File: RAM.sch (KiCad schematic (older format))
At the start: 14 parts, among them U35 74HC00, U36 74LS245, U37 74HC04, U38 74LS173, U39 74LS173, U40 74LS245, U41 74LS173, U42 74LS173, U43 AS6C6264, U44 AS6C6264, U45 AT28C64B-15PU, U46 AT28C64B-15PU

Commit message: non floating ram and ir , added stack register
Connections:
- no-connect marks 5 -> 23
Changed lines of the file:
@@
 $Descr A2 23386 16535
 encoding utf-8
-Sheet 7 9
+Sheet 7 10
 Title ""
 Date ""
@@
 	6850 4850 6850 4950
 Wire Wire Line
-	9500 4950 9500 4850
-Wire Wire Line
 	7950 5200 7950 2000
-Wire Wire Line
-	6850 4950 9500 4950
 Connection ~ 6150 1700
 Wire Wire Line
@@
 	3600 7450 3600 5750
 Wire Wire Line
-	9200 6050 9200 5100
-Connection ~ 9500 4950
-Wire Wire Line
-	9400 5000 6750 5000
-Wire Wire Line
 	9600 5000 9400 5000
-Connection ~ 9400 5000
-Wire Wire Line
-	9300 5050 9700 5050
-Wire Wire Line
-	6650 5050 9300 5050
-Connection ~ 9300 5050
-Wire Wire Line
-	9400 5300 9400 5000
-Wire Wire Line
-	9500 5300 9500 4950
 Wire Wire Line
 	11250 7550 11250 7250
@@
 	8650 10150 8650 12400
 Wire Wire Line
-	9300 5050 9300 5900
-Wire Wire Line
 	9300 7850 11800 7850
 $Comp
@@
 Wire Wire Line
 	10000 5000 11750 5000
-Connection ~ 9300 5900
 Wire Wire Line
 	9300 5900 9300 7850
@@
 Wire Wire Line
 	10750 3400 10750 6250
-NoConn ~ 9200 6050
 Wire Wire Line
 	10950 3400 10950 2700
@@
 NoConn ~ 10250 8150
 NoConn ~ 10250 8650
+Wire Wire Line
+	9200 5900 9300 5900
+Wire Wire Line
+	9200 5900 9200 5100
+Connection ~ 9300 5900
+Wire Wire Line
+	9300 5050 9700 5050
+Wire Wire Line
+	9300 5550 9400 5550
+Wire Wire Line
+	9400 5000 9400 5550
+Wire Wire Line
+	9300 5050 9300 5550
+Wire Wire Line
+	9500 5550 9400 5550
+Connection ~ 9400 5550
+Wire Wire Line
+	9400 5550 9400 5750
+$Comp
+L 16bitCpu-rescue:GND-power #PWR?
+U 1 1 60F07EDE
+P 9400 5750
+F 0 "#PWR?" H 9400 5500 50  0001 C CNN
+F 1 "GND-power" H 9488 5713 50  0000 L CNN
+F 2 "" H 9400 5750 50  0001 C CNN
+F 3 "" H 9400 5750 50  0001 C CNN
+	1    9400 5750
+	1    0    0    -1
+$EndComp
+Wire Wire Line
+	9500 4850 9500 5550
+NoConn ~ 6650 5050
+NoConn ~ 6750 5000
+NoConn ~ 6850 4950
+NoConn ~ 22700 900
+NoConn ~ 22700 1000
+NoConn ~ 22700 1100
+NoConn ~ 22700 1200
+NoConn ~ 22700 1300
+NoConn ~ 22700 1400
+NoConn ~ 22700 1500
+NoConn ~ 22700 1600
+NoConn ~ 22700 1700
+NoConn ~ 22700 1800
+NoConn ~ 22700 1900
+NoConn ~ 22700 2000
+NoConn ~ 22700 2100
+NoConn ~ 22700 2200
+NoConn ~ 22700 2300
+NoConn ~ 22700 2400
 $EndSCHEMATC

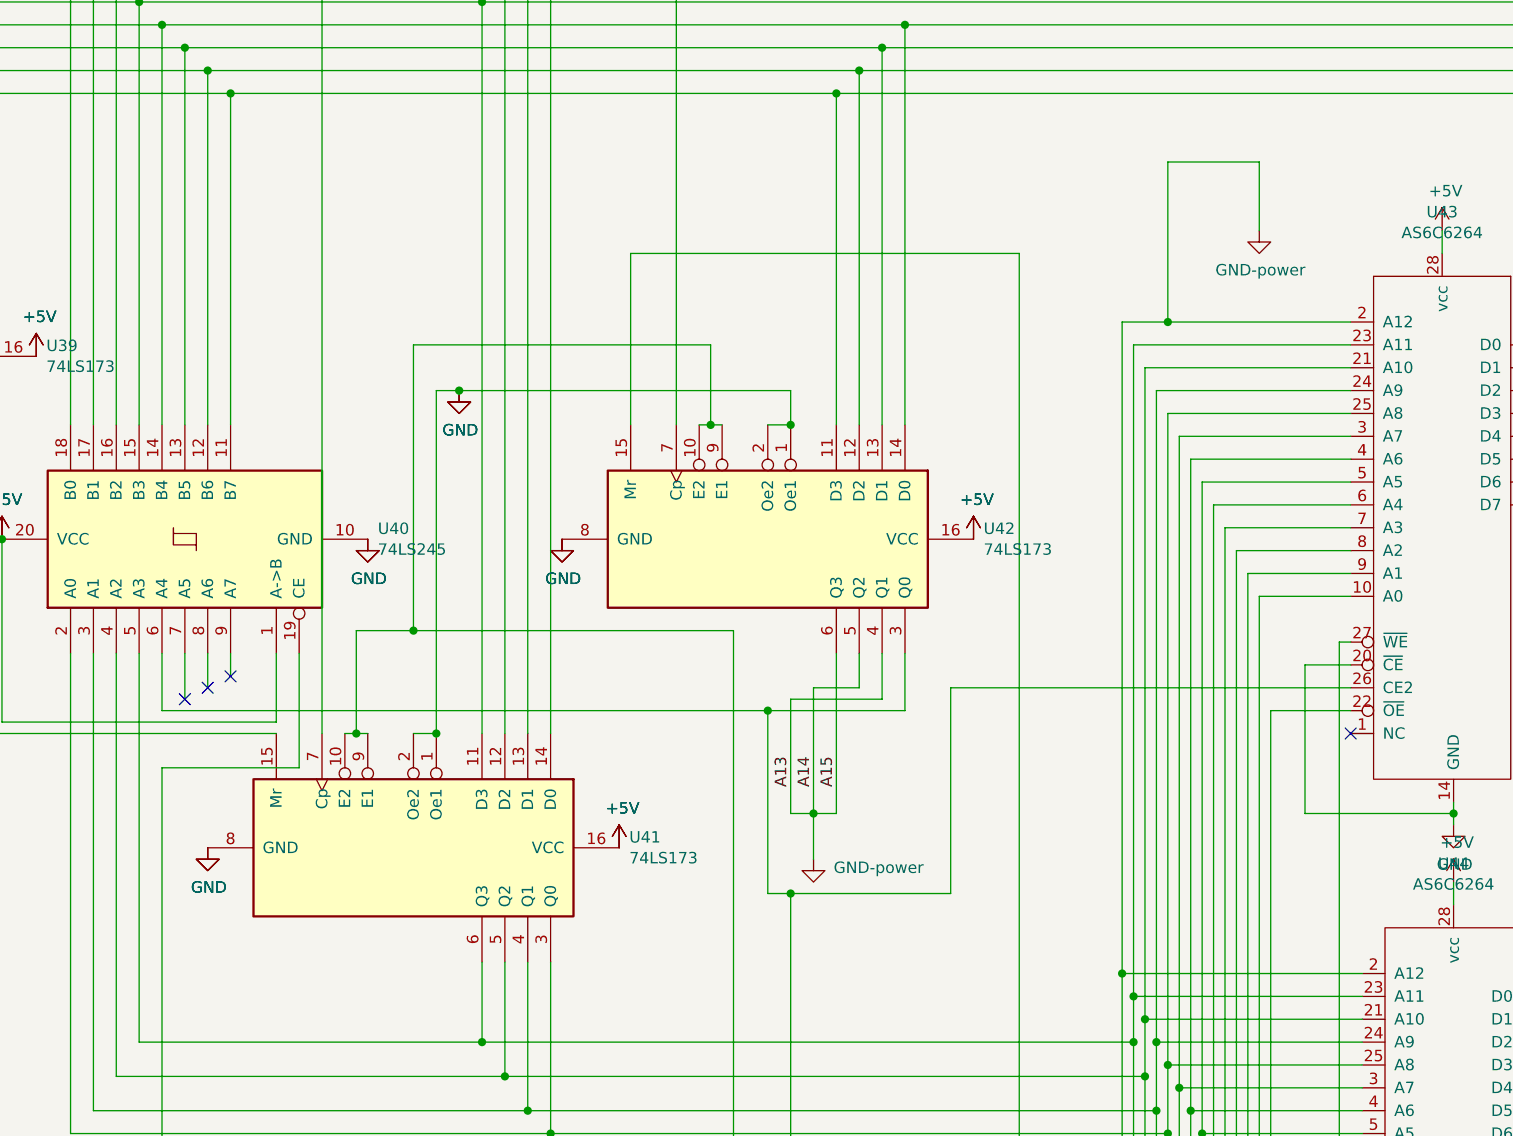
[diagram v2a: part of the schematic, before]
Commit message: back to 13 bit addresses
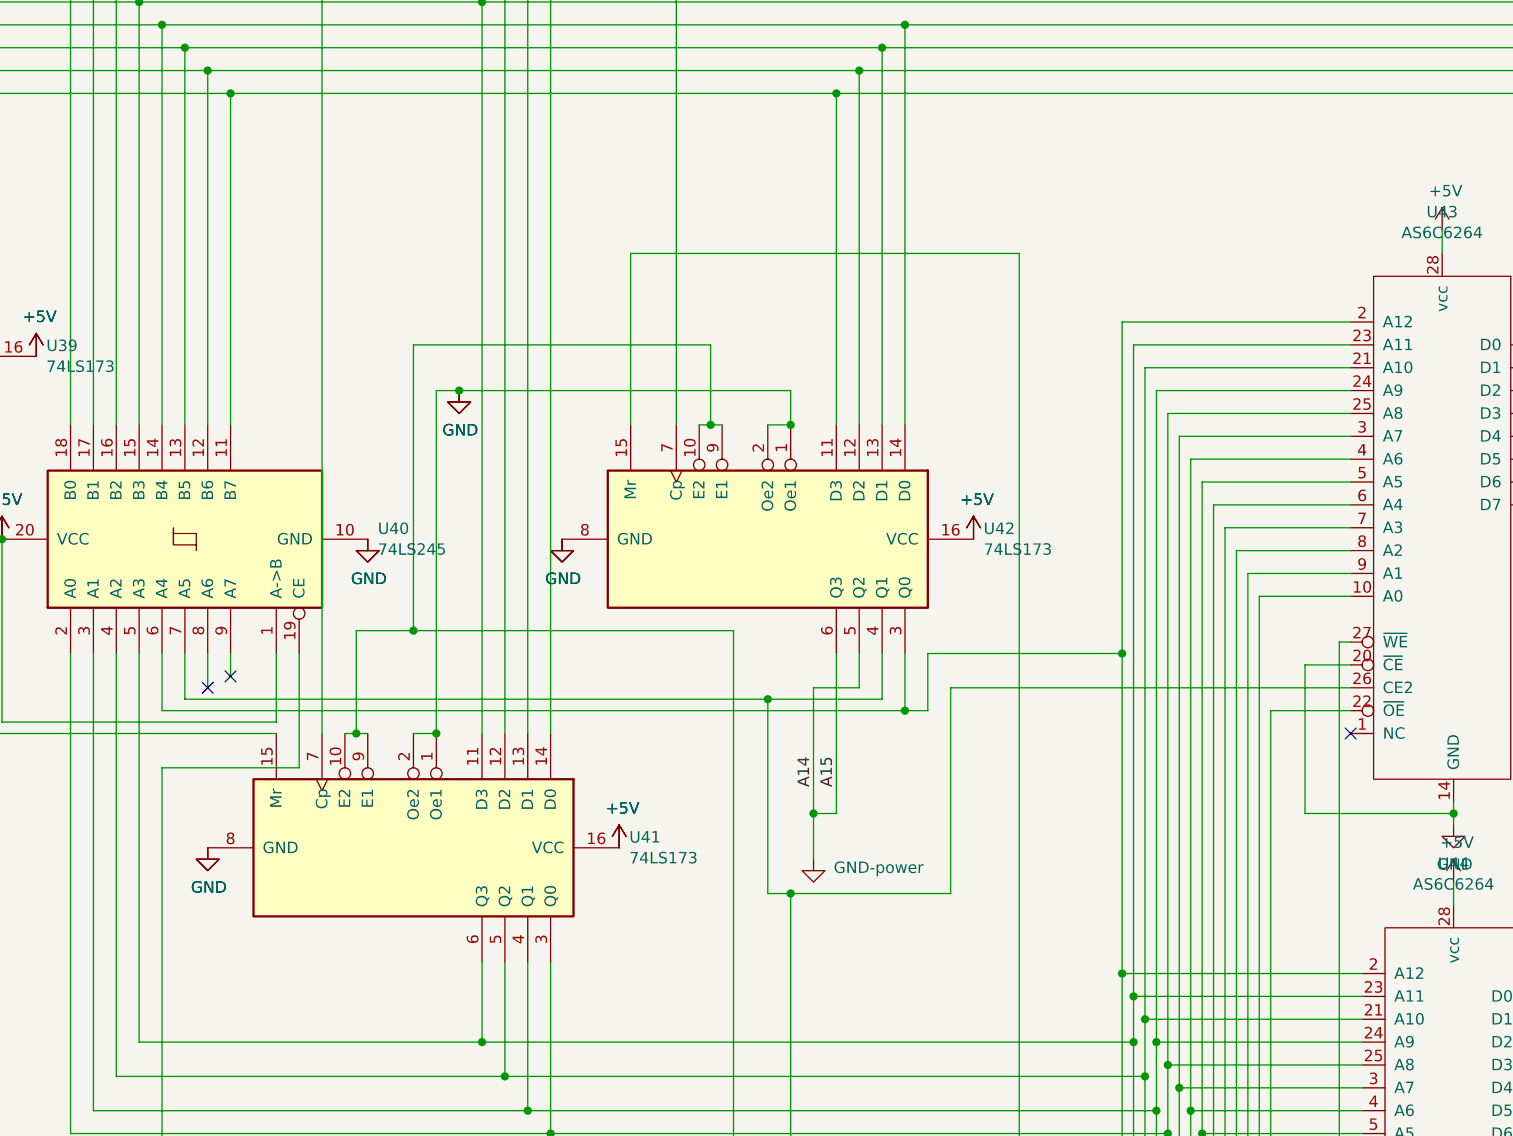
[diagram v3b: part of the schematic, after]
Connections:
- net GND: no longer U42.4 (Q1), U43.2 (A12), U44.2 (A12), U45.2 (A12), U46.2 (A12)
- net at U43.26 (CE2), U44.26 (CE2), U45.20 (~CE~)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: now also U40.7 (A5), U42.4 (Q1); no longer U40.6 (A4), U42.3 (Q0)
- new net: U40.6 (A4), U42.3 (Q0), U43.2 (A12), U44.2 (A12), U45.2 (A12), U46.2 (A12)
- no-connect marks 23 -> 22
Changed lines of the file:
@@
 Wire Wire Line
 	5000 4300 5700 4300
-Wire Wire Line
-	6550 5100 9200 5100
-Connection ~ 9200 5100
-Wire Wire Line
-	9200 5100 9800 5100
 $Comp
 L 16bitCpu-rescue:+5V-power #PWR?
@@
 	1    0    0    -1
 $EndComp
-$Comp
-L draguve:AS6C6264 U43
-U 1 1 5F6F3976
-P 11650 4500
-F 0 "U43" H 12150 6081 50  0000 C CNN
-F 1 "AS6C6264" H 12150 5990 50  0000 C CNN
-F 2 "Package_DIP:DIP-28_W15.24mm" H 12300 6200 50  0001 C CNN
-F 3 "" H 12300 6200 50  0001 C CNN
-	1    11650 4500
-	1    0    0    -1
-$EndComp
 Wire Wire Line
 	8800 650  15800 650
-Wire Wire Line
-	10750 3400 10950 3400
 Wire Wire Line
 	10750 6250 11800 6250
@@
 Wire Wire Line
 	11350 7450 11350 4600
-Text Label 9300 5300 3    50   ~ 0
-A13
 Text Label 9400 5300 3    50   ~ 0
 A14
@@
 Wire Wire Line
 	11750 4900 11550 4900
-Wire Wire Line
-	11550 5550 12200 5550
 Wire Wire Line
 	11800 7750 11600 7750
@@
 Wire Wire Line
 	12200 5950 12200 5850
-Wire Wire Line
-	11550 4900 11550 5550
-Wire Wire Line
-	12200 5500 12200 5550
 $Comp
 L 16bitCpu-rescue:GND-power #PWR0135
@@
 	12250 8400 12250 8450
 Connection ~ 12250 8400
-Wire Wire Line
-	12200 5550 12200 5600
-Connection ~ 12200 5550
 NoConn ~ 11800 8050
 NoConn ~ 11750 5200
@@
 	10000 5900 9300 5900
 Wire Wire Line
-	10000 5000 11750 5000
-Wire Wire Line
 	9300 5900 9300 7850
-Wire Wire Line
-	12150 3000 12150 3100
 $Comp
 L 16bitCpu-rescue:GND-power #PWR0132
@@
 $EndComp
 Wire Wire Line
-	10750 3400 10750 6250
-Wire Wire Line
-	10950 3400 10950 2700
-Wire Wire Line
-	10950 2700 11350 2700
-Wire Wire Line
-	11350 2700 11350 3000
-Connection ~ 10950 3400
-Wire Wire Line
-	10950 3400 11750 3400
-$Comp
-L 16bitCpu-rescue:GND-power #PWR0181
-U 1 1 5FAE8C08
-P 11350 3000
-F 0 "#PWR0181" H 11350 2750 50  0001 C CNN
-F 1 "GND-power" H 11355 2827 50  0000 C CNN
-F 2 "" H 11350 3000 50  0001 C CNN
-F 3 "" H 11350 3000 50  0001 C CNN
-	1    11350 3000
-	1    0    0    -1
-$EndComp
+	10750 3400 10750 4850
 NoConn ~ 10250 8150
 NoConn ~ 10250 8650
 Wire Wire Line
-	9200 5900 9300 5900
-Wire Wire Line
-	9200 5900 9200 5100
-Connection ~ 9300 5900
-Wire Wire Line
-	9300 5050 9700 5050
-Wire Wire Line
-	9300 5550 9400 5550
-Wire Wire Line
 	9400 5000 9400 5550
-Wire Wire Line
-	9300 5050 9300 5550
 Wire Wire Line
 	9500 5550 9400 5550
@@
 Wire Wire Line
 	9500 4850 9500 5550
-NoConn ~ 6650 5050
 NoConn ~ 6750 5000
 NoConn ~ 6850 4950
@@
 NoConn ~ 22700 2300
 NoConn ~ 22700 2400
+Connection ~ 9300 5900
+Wire Wire Line
+	9200 5900 9300 5900
+Wire Wire Line
+	9700 5050 9200 5050
+Wire Wire Line
+	6550 5100 9800 5100
+Wire Wire Line
+	9200 5900 9200 5050
+Connection ~ 9200 5050
+Wire Wire Line
+	9200 5050 6650 5050
+Wire Wire Line
+	9800 5100 9900 5100
+Wire Wire Line
+	9900 5100 9900 4850
+Wire Wire Line
+	9900 4850 10750 4850
+Connection ~ 9800 5100
+Connection ~ 10750 4850
+Wire Wire Line
+	10750 4850 10750 6250
+Wire Wire Line
+	10750 3400 11750 3400
+$Comp
+L draguve:AS6C6264 U43
+U 1 1 5F6F3976
+P 11650 4500
+F 0 "U43" H 12150 6081 50  0000 C CNN
+F 1 "AS6C6264" H 12150 5990 50  0000 C CNN
+F 2 "Package_DIP:DIP-28_W15.24mm" H 12300 6200 50  0001 C CNN
+F 3 "" H 12300 6200 50  0001 C CNN
+	1    11650 4500
+	1    0    0    -1
+$EndComp
+Wire Wire Line
+	12200 5500 12200 5550
+Wire Wire Line
+	12200 5550 12200 5600
+Connection ~ 12200 5550
+Wire Wire Line
+	11550 5550 12200 5550
+Wire Wire Line
+	12150 3000 12150 3100
+Wire Wire Line
+	10000 5000 11750 5000
+Wire Wire Line
+	11550 4900 11550 5550
 $EndSCHEMATC

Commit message: Let there be light
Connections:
- net sheet61B5B12C/I0: now reaches U36.2 (A0), U38.3 (Q0), U43.10 (A0), U44.10 (A0), U45.10 (A0), U46.10 (A0)
- net sheet61B5B12C/I1: now reaches U36.3 (A1), U38.4 (Q1), U43.9 (A1), U44.9 (A1), U45.9 (A1), U46.9 (A1)
- net sheet61B5B12C/I2: now reaches U36.4 (A2), U38.5 (Q2), U43.8 (A2), U44.8 (A2), U45.8 (A2), U46.8 (A2)
- net sheet61B5B12C/I3: now reaches U36.5 (A3), U38.6 (Q3), U43.7 (A3), U44.7 (A3), U45.7 (A3), U46.7 (A3)
- net sheet61B5B12C/I4: now reaches U36.6 (A4), U39.3 (Q0), U43.6 (A4), U44.6 (A4), U45.6 (A4), U46.6 (A4)
- net sheet61B5B12C/I5: now reaches U36.7 (A5), U39.4 (Q1), U43.5 (A5), U44.5 (A5), U45.5 (A5), U46.5 (A5)
- net sheet61B5B12C/I6: now reaches U36.8 (A6), U39.5 (Q2), U43.4 (A6), U44.4 (A6), U45.4 (A6), U46.4 (A6)
- net sheet61B5B12C/I7: now reaches U36.9 (A7), U39.6 (Q3), U43.3 (A7), U44.3 (A7), U45.3 (A7), U46.3 (A7)
- net sheet61B5B12C/I12: now reaches U40.6 (A4), U42.3 (Q0), U43.2 (A12), U44.2 (A12), U45.2 (A12), U46.2 (A12)
- net sheet61B5B12C/I13: now reaches U40.7 (A5), U42.4 (Q1), U43.26 (CE2), U44.26 (CE2), U45.20 (~CE~), U46.20 (~CE~)
- net sheet61B5B12C/I8: now reaches U40.2 (A0), U41.3 (Q0), U43.25 (A8), U44.25 (A8), U45.25 (A8), U46.25 (A8)
- net sheet61B5B12C/I9: now reaches U40.3 (A1), U41.4 (Q1), U43.24 (A9), U44.24 (A9), U45.24 (A9), U46.24 (A9)
- net sheet61B5B12C/I10: now reaches U40.4 (A2), U41.5 (Q2), U43.21 (A10), U44.21 (A10), U45.21 (A10), U46.21 (A10)
